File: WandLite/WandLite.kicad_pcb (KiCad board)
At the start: 2 copper layers, 13 x 39.8 mm, 11 parts, among them J10 VCC-O, J11 PB1-O, J12 PB0-O, J13 GND-O, J14 VCC-I, J3 PB2-MDDN, J5 PB3-MDUP, J6 PB4-TRIG, J7 GND-C, J8 GND-I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

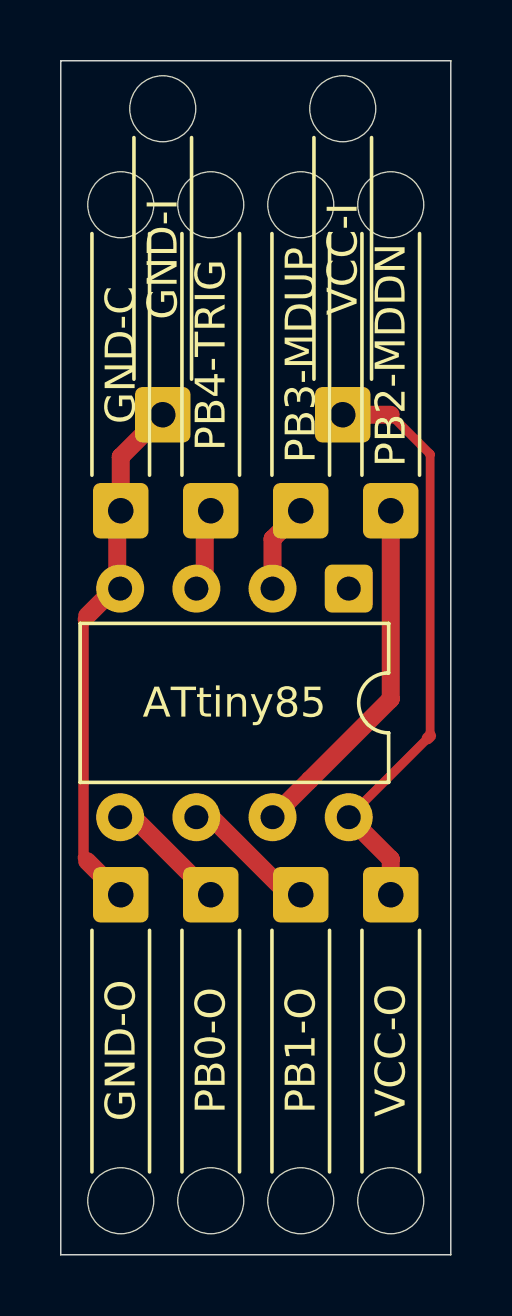
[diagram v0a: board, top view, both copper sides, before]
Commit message: inside routed to save some width
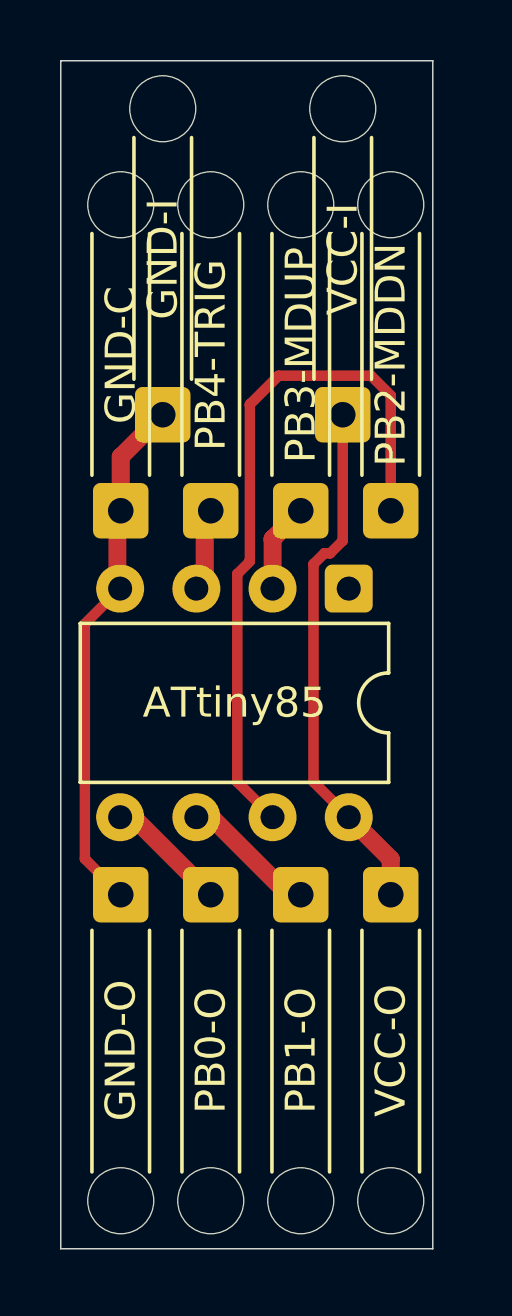
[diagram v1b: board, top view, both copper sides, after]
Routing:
- net Net-(J3-Pin_1): track 12.9 -> 23.6 mm
- net VCC: track 19.8 -> 17.6 mm
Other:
- board size 13 x 39.8 mm -> 12.4 x 39.6 mm
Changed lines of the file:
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@@
 		)
 		(property "Value" "PB2-MDDN"
-			(at 0 5.19 90)
+			(at 0 5.2 90)
 			(layer "F.SilkS")
 			(effects
@@
 	(gr_rect
 		(start 131.8 56.6)
-		(end 144.800728 96.4)
+		(end 144.200728 96.2)
 		(stroke
 			(width 0.05)
@@
 	)
 	(segment
-		(start 140.0958 80.5792)
+		(start 138.101 68.056774)
+		(end 138.101 73.290884)
+		(width 0.35)
+		(layer "F.Cu")
+		(net 1)
+	)
+	(segment
+		(start 137.684 73.707884)
+		(end 137.684 80.639)
+		(width 0.35)
+		(layer "F.Cu")
+		(net 1)
+	)
+	(segment
+		(start 142.8 67.757774)
+		(end 142.141226 67.099)
+		(width 0.35)
+		(layer "F.Cu")
+		(net 1)
+	)
+	(segment
+		(start 142.8 71.6)
+		(end 142.8 67.757774)
+		(width 0.35)
+		(layer "F.Cu")
+		(net 1)
+	)
+	(segment
+		(start 139.058774 67.099)
+		(end 138.101 68.056774)
+		(width 0.35)
+		(layer "F.Cu")
+		(net 1)
+	)
+	(segment
+		(start 142.141226 67.099)
+		(end 139.058774 67.099)
+		(width 0.35)
+		(layer "F.Cu")
+		(net 1)
+	)
+	(segment
+		(start 137.684 80.639)
 		(end 138.86 81.815)
-		(width 0.6)
+		(width 0.35)
 		(layer "F.Cu")
 		(net 1)
 	)
 	(segment
-		(start 142.8 71.6)
-		(end 142.0524 71.6)
-		(width 0.2)
-		(layer "F.Cu")
-		(net 1)
-	)
-	(segment
-		(start 142.8 77.875)
-		(end 140.0958 80.5792)
-		(width 0.6)
-		(layer "F.Cu")
-		(net 1)
-	)
-	(segment
-		(start 142.8 72.3476)
-		(end 142.8 77.875)
-		(width 0.6)
-		(layer "F.Cu")
-		(net 1)
-	)
-	(segment
-		(start 142.0524 71.6)
-		(end 142.8 72.3476)
+		(start 138.101 73.290884)
+		(end 137.684 73.707884)
 		(width 0.35)
 		(layer "F.Cu")
@@
 	)
 	(segment
-		(start 132.560815 83.160815)
-		(end 132.6783 83.2783)
-		(width 0.4)
-		(layer "F.Cu")
-		(net 4)
-	)
-	(segment
-		(start 132.6783 83.2783)
-		(end 133.8 84.4)
-		(width 0.6)
+		(start 132.604 75.371)
+		(end 132.604 83.204)
+		(width 0.35)
 		(layer "F.Cu")
 		(net 4)
@@
 	)
 	(segment
-		(start 133.59 74.195)
-		(end 132.6783 75.1067)
-		(width 0.6)
+		(start 132.604 83.204)
+		(end 133.8 84.4)
+		(width 0.35)
 		(layer "F.Cu")
 		(net 4)
@@
 	)
 	(segment
-		(start 132.6783 75.1067)
-		(end 132.560815 75.224185)
-		(width 0.4)
+		(start 133.78 74.195)
+		(end 132.604 75.371)
+		(width 0.35)
 		(layer "F.Cu")
 		(net 4)
@@
 	)
 	(segment
-		(start 132.560815 75.224185)
-		(end 132.560815 83.160815)
-		(width 0.35)
-		(layer "F.Cu")
-		(net 4)
-	)
-	(segment
 		(start 133.685 71.715)
 		(end 133.685 74.1)
@@
 	)
 	(segment
-		(start 144.112892 69.713621)
-		(end 142.799271 68.4)
-		(width 0.3)
-		(layer "F.Cu")
-		(net 5)
-	)
-	(segment
 		(start 142.8 83.215)
 		(end 141.4 81.815)
@@
 	)
 	(segment
-		(start 141.7594 68.4)
-		(end 141.2 68.4)
-		(width 0.2)
+		(start 140.224 80.639)
+		(end 141.4 81.815)
+		(width 0.35)
 		(layer "F.Cu")
 		(net 5)
 	)
 	(segment
-		(start 141.4 81.815)
-		(end 144.0277 79.1873)
-		(width 0.3)
+		(start 140.224 73.378774)
+		(end 140.224 80.639)
+		(width 0.35)
 		(layer "F.Cu")
 		(net 5)
 	)
 	(segment
-		(start 144.112892 79.102108)
-		(end 144.112892 69.713621)
-		(width 0.3)
+		(start 140.583774 73.019)
+		(end 140.224 73.378774)
+		(width 0.35)
 		(layer "F.Cu")
 		(net 5)
 	)
 	(segment
-		(start 142.799271 68.4)
-		(end 141.7594 68.4)
-		(width 0.6)
+		(start 141.2 72.6)
+		(end 140.781 73.019)
+		(width 0.35)
 		(layer "F.Cu")
 		(net 5)
@@
 	)
 	(segment
-		(start 144.0277 79.1873)
-		(end 144.112892 79.102108)
-		(width 0.4)
+		(start 140.781 73.019)
+		(end 140.583774 73.019)
+		(width 0.35)
 		(layer "F.Cu")
 		(net 5)
@@
 		(layer "F.Cu")
 		(net 5)
+	)
+	(segment
+		(start 141.2 68.4)
+		(end 141.2 72.6)
+		(width 0.35)
+		(layer "F.Cu")
+		(net 5)

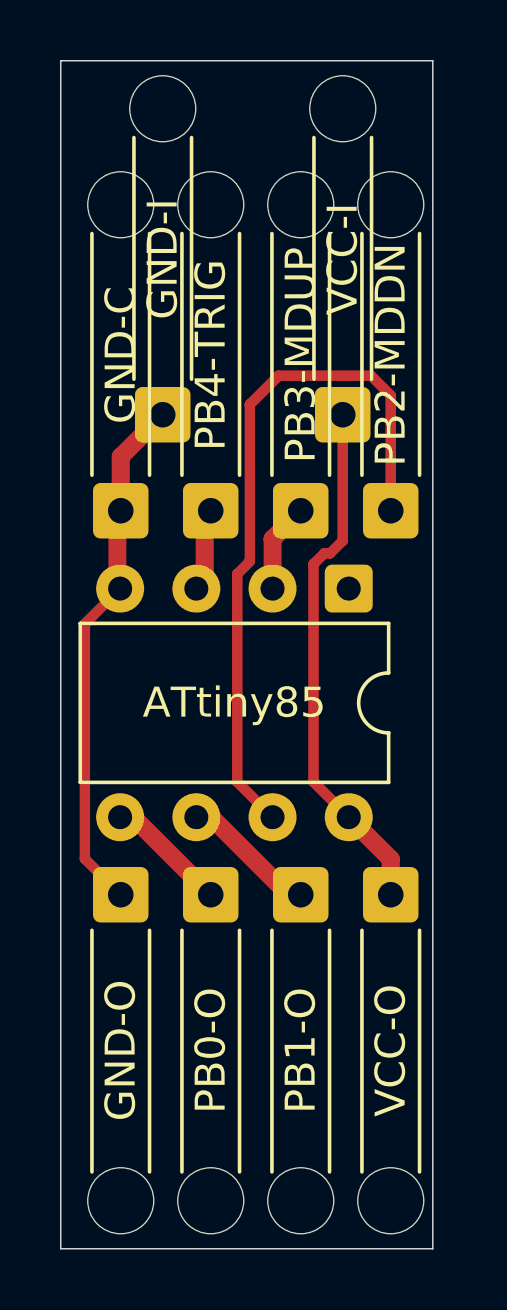
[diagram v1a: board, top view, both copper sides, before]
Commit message: short relief and output
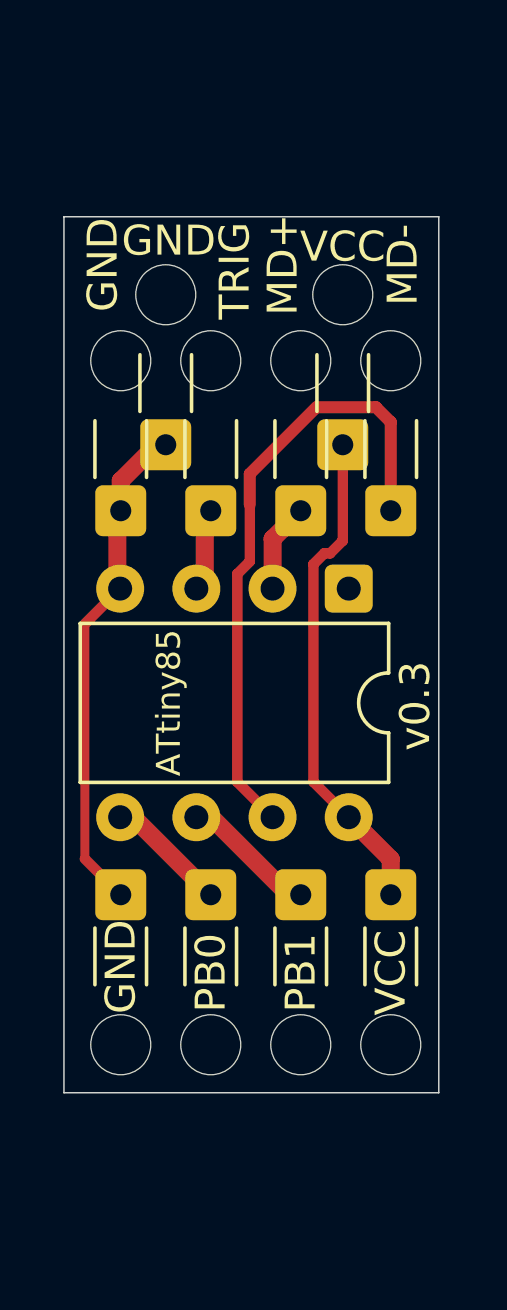
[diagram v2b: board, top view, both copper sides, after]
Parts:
- GND: renamed from J7; footprint Connector_Wire:SolderWire-0.25sqmm_1x01_D0.65mm_OD1.7mm_Relief -> Kelvin_Library:SolderWire-0.15sqmm_1x01_D0.5mm_OD1.5mm_Relief_SHORT
- GND: renamed from J8; footprint Connector_Wire:SolderWire-0.25sqmm_1x01_D0.65mm_OD1.7mm_Relief -> Kelvin_Library:SolderWire-0.15sqmm_1x01_D0.5mm_OD1.5mm_Relief_SHORT
- GND: renamed from J13; footprint Connector_Wire:SolderWire-0.25sqmm_1x01_D0.65mm_OD1.7mm_Relief -> Kelvin_Library:SolderWire-0.15sqmm_1x01_D0.5mm_OD1.5mm_Relief_SHORT
- MD+: renamed from J5; footprint Connector_Wire:SolderWire-0.25sqmm_1x01_D0.65mm_OD1.7mm_Relief -> Kelvin_Library:SolderWire-0.15sqmm_1x01_D0.5mm_OD1.5mm_Relief_SHORT
- MD-: renamed from J3; footprint Connector_Wire:SolderWire-0.25sqmm_1x01_D0.65mm_OD1.7mm_Relief -> Kelvin_Library:SolderWire-0.15sqmm_1x01_D0.5mm_OD1.5mm_Relief_SHORT
- PB0: renamed from J12; footprint Connector_Wire:SolderWire-0.25sqmm_1x01_D0.65mm_OD1.7mm_Relief -> Kelvin_Library:SolderWire-0.15sqmm_1x01_D0.5mm_OD1.5mm_Relief_SHORT
- PB1: renamed from J11; footprint Connector_Wire:SolderWire-0.25sqmm_1x01_D0.65mm_OD1.7mm_Relief -> Kelvin_Library:SolderWire-0.15sqmm_1x01_D0.5mm_OD1.5mm_Relief_SHORT
- TRIG: renamed from J6; footprint Connector_Wire:SolderWire-0.25sqmm_1x01_D0.65mm_OD1.7mm_Relief -> Kelvin_Library:SolderWire-0.15sqmm_1x01_D0.5mm_OD1.5mm_Relief_SHORT
- VCC: renamed from J10; footprint Connector_Wire:SolderWire-0.25sqmm_1x01_D0.65mm_OD1.7mm_Relief -> Kelvin_Library:SolderWire-0.15sqmm_1x01_D0.5mm_OD1.5mm_Relief_SHORT
- VCC: renamed from J14; footprint Connector_Wire:SolderWire-0.25sqmm_1x01_D0.65mm_OD1.7mm_Relief -> Kelvin_Library:SolderWire-0.15sqmm_1x01_D0.5mm_OD1.5mm_Relief_SHORT
- moved GND 1.00 mm to (135.3, 69.4)
- moved VCC 1.00 mm to (141.2, 69.4)
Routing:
- net Net-(J3-Pin_1): track 23.6 -> 20.9 mm
- net VCC: track 17.6 -> 16.6 mm
- net GND: track 18.1 -> 17.3 mm
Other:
- board size 12.4 x 39.6 mm -> 12.5 x 29.2 mm
- board text added: "v0.3"

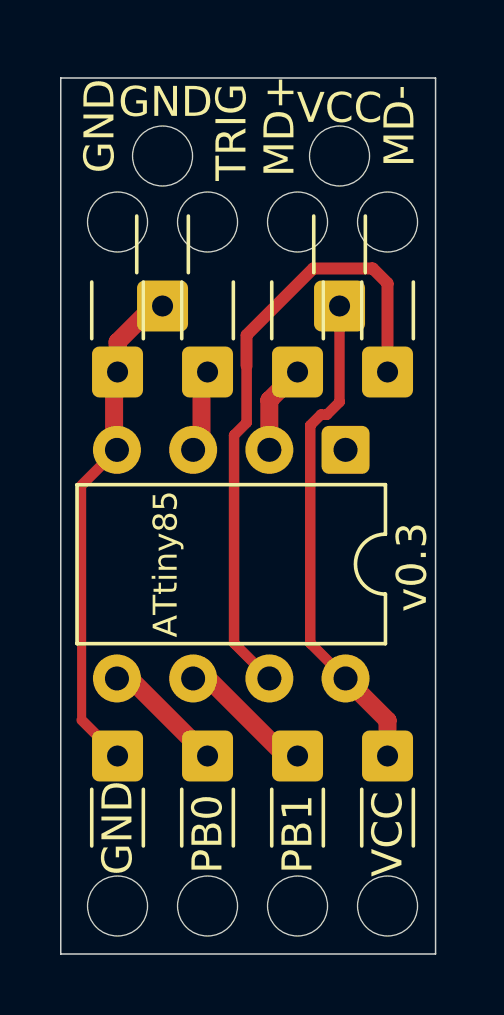
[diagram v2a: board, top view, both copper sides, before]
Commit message: removed mode- for vcc-c
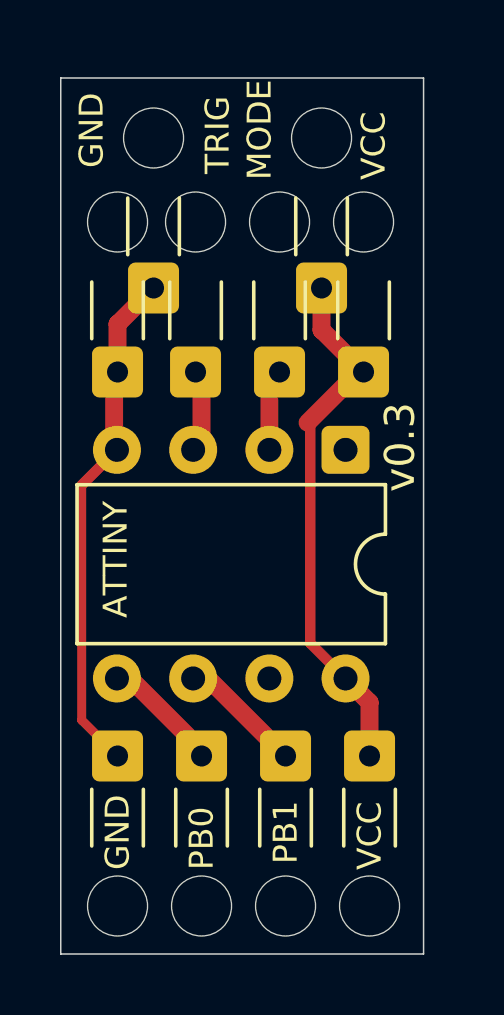
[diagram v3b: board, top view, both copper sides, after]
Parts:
- removed GND: GND-C, Kelvin_Library:SolderWire-0.15sqmm_1x01_D0.5mm_OD1.5mm_Relief_SHORT
- removed GND: GND-I, Kelvin_Library:SolderWire-0.15sqmm_1x01_D0.5mm_OD1.5mm_Relief_SHORT
- removed GND: GND-O, Kelvin_Library:SolderWire-0.15sqmm_1x01_D0.5mm_OD1.5mm_Relief_SHORT
- removed MD+: PB3-MDUP, Kelvin_Library:SolderWire-0.15sqmm_1x01_D0.5mm_OD1.5mm_Relief_SHORT
- removed MD-: PB2-MDDN, Kelvin_Library:SolderWire-0.15sqmm_1x01_D0.5mm_OD1.5mm_Relief_SHORT
- removed TRIG: PB4-TRIG, Kelvin_Library:SolderWire-0.15sqmm_1x01_D0.5mm_OD1.5mm_Relief_SHORT
- removed VCC: VCC-O, Kelvin_Library:SolderWire-0.15sqmm_1x01_D0.5mm_OD1.5mm_Relief_SHORT
- removed VCC: VCC-I, Kelvin_Library:SolderWire-0.15sqmm_1x01_D0.5mm_OD1.5mm_Relief_SHORT
- added GND-C1: GND-C, Kelvin_Library:SolderWire-0.15sqmm_1x01_D0.5mm_OD1.5mm_Relief_SHORT, F.Cu at (133.8, 71.6)
- added GND-I1: GND-I, Kelvin_Library:SolderWire-0.15sqmm_1x01_D0.5mm_OD1.5mm_Relief_SHORT, F.Cu at (135.0, 68.8)
- added GND-O1: GND-O, Kelvin_Library:SolderWire-0.15sqmm_1x01_D0.5mm_OD1.5mm_Relief_SHORT, F.Cu at (133.8, 84.4)
- added MD+1: PB3-MDUP, Kelvin_Library:SolderWire-0.15sqmm_1x01_D0.5mm_OD1.5mm_Relief_SHORT, F.Cu at (139.2, 71.6)
- added TRIG1: PB4-TRIG, Kelvin_Library:SolderWire-0.15sqmm_1x01_D0.5mm_OD1.5mm_Relief_SHORT, F.Cu at (136.4, 71.6)
- added VCC-C1: VCC-C, Kelvin_Library:SolderWire-0.15sqmm_1x01_D0.5mm_OD1.5mm_Relief_SHORT, F.Cu at (142.0, 71.6)
- added VCC-I1: VCC-I, Kelvin_Library:SolderWire-0.15sqmm_1x01_D0.5mm_OD1.5mm_Relief_SHORT, F.Cu at (140.6, 68.8)
- added VCC-O1: VCC-O, Kelvin_Library:SolderWire-0.15sqmm_1x01_D0.5mm_OD1.5mm_Relief_SHORT, F.Cu at (142.2, 84.4)
- U1: value ATtiny85 -> ATtiny85-20P
- moved PB1 0.40 mm to (139.4, 84.4)
- moved PB0 0.20 mm to (136.6, 84.4)
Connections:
- U1 pad 7: Net-(J3-Pin_1) -> unconnected-(U1-PB2-Pad7)
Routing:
- net Net-(J3-Pin_1): track 20.9 -> 0.00 mm
- net Net-(MD+1-Pin_1): track 2.98 -> 1.65 mm
- net VCC: track 16.6 -> 17.6 mm
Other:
- board size 12.5 x 29.2 mm -> 12.1 x 29.2 mm
- board text added: "ATTINY"
- board text added: "GND"
- board text added: "MODE"
- board text added: "PB0"
- board text added: "PB1"
- board text added: "TRIG"
- board text added: "VCC"

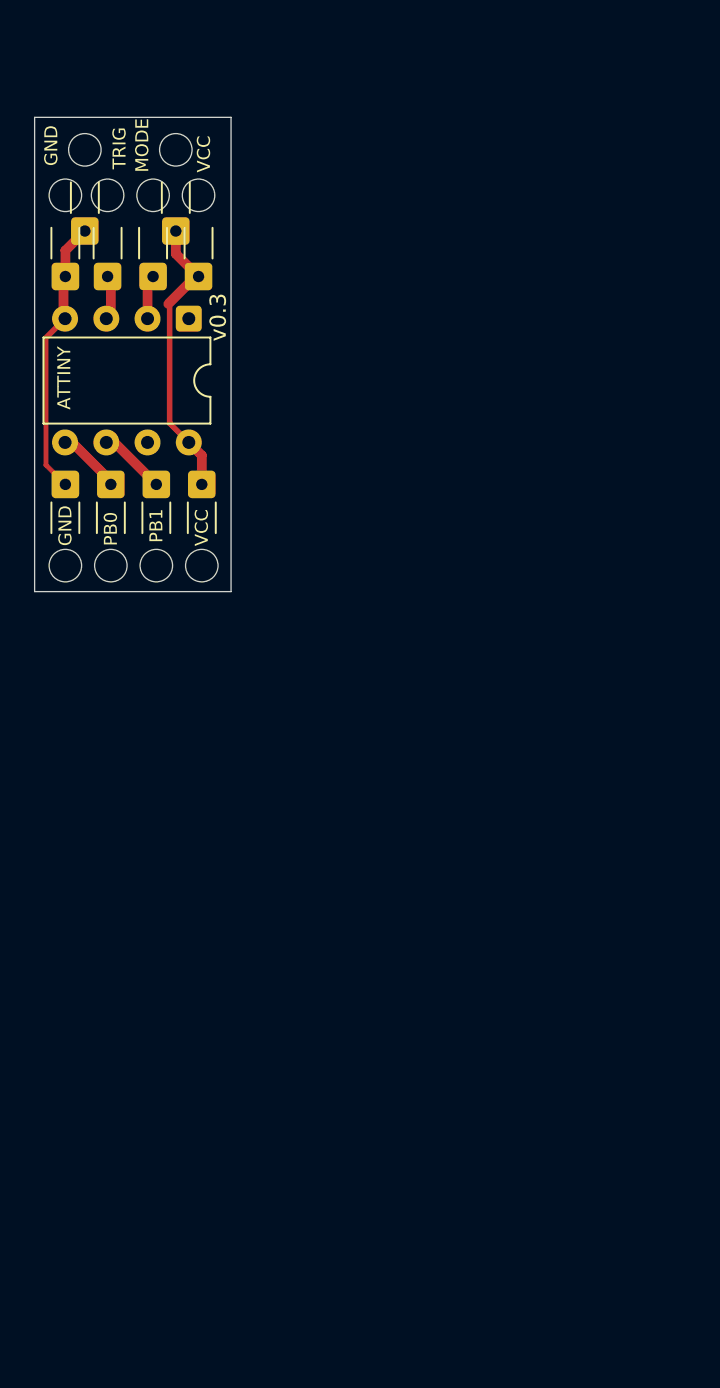
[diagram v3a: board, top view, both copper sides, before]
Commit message: removed mode- for vcc-c
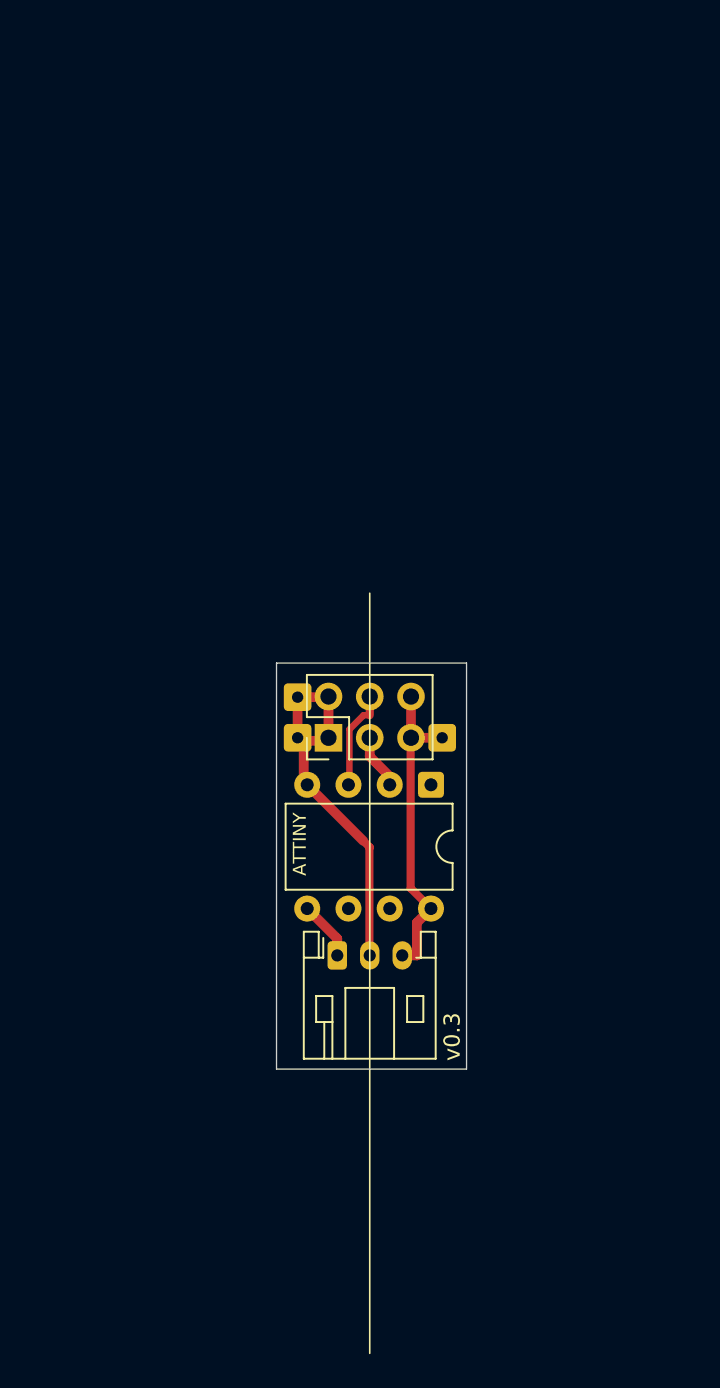
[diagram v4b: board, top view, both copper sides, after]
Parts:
- removed GND-C1: GND-C, Kelvin_Library:SolderWire-0.15sqmm_1x01_D0.5mm_OD1.5mm_Relief_SHORT
- removed GND-O1: GND-O, Kelvin_Library:SolderWire-0.15sqmm_1x01_D0.5mm_OD1.5mm_Relief_SHORT
- removed MD+1: PB3-MDUP, Kelvin_Library:SolderWire-0.15sqmm_1x01_D0.5mm_OD1.5mm_Relief_SHORT
- removed PB0: PB0-O, Kelvin_Library:SolderWire-0.15sqmm_1x01_D0.5mm_OD1.5mm_Relief_SHORT
- removed PB1: PB1-O, Kelvin_Library:SolderWire-0.15sqmm_1x01_D0.5mm_OD1.5mm_Relief_SHORT
- removed TRIG1: PB4-TRIG, Kelvin_Library:SolderWire-0.15sqmm_1x01_D0.5mm_OD1.5mm_Relief_SHORT
- removed VCC-C1: VCC-C, Kelvin_Library:SolderWire-0.15sqmm_1x01_D0.5mm_OD1.5mm_Relief_SHORT
- removed VCC-O1: VCC-O, Kelvin_Library:SolderWire-0.15sqmm_1x01_D0.5mm_OD1.5mm_Relief_SHORT
- added BLD-O1: Conn_01x03_Pin, Connector_JST:JST_PH_S3B-PH-K_1x03_P2.00mm_Horizontal, F.Cu at (150.5, 113.4)
- added GND-I2: Conn_01x01, Connector_Wire:SolderWire-0.15sqmm_1x01_D0.5mm_OD1.5mm, F.Cu at (148.1, 100.0)
- added J-IN1: Conn_02x03_Odd_Even, Connector_PinHeader_2.54mm:PinHeader_2x03_P2.54mm_Vertical, F.Cu at (150.0, 100.0)
- GND-I1, VCC-I1: footprint Kelvin_Library:SolderWire-0.15sqmm_1x01_D0.5mm_OD1.5mm_Relief_SHORT -> Connector_Wire:SolderWire-0.15sqmm_1x01_D0.5mm_OD1.5mm
- moved VCC-I1 35.2 mm to (157.0, 100.0), turned to 0 degrees
- moved U1 32.3 mm to (156.3, 102.9)
- moved GND-I1 31.5 mm to (148.1, 97.5), turned to 0 degrees
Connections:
- U1 pad 6: Net-(PB1-Pin_1) -> unconnected-(U1-PB1-Pad6)
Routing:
- net GND: track 17.5 -> 24.5 mm
- net Net-(PB1-Pin_1): track 4.15 -> 0.00 mm
- net Net-(J-IN1-Pin_4): track 2.84 -> 6.20 mm
- net VCC: track 17.6 -> 19.6 mm
- net Net-(J-IN1-Pin_3): track 1.65 -> 3.40 mm
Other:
- board size 12.1 x 29.2 mm -> 11.7 x 25 mm
- board text removed: "GND"
- board text removed: "MODE"
- board text removed: "PB0"
- board text removed: "PB1"
- board text removed: "TRIG"
- board text removed: "VCC"
